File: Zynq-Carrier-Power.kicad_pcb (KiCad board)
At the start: 2 copper layers, 49 x 41 mm, 36 parts, among them J1 Zynq_SoM, J10 Barrel_Jack_MountingPin, J2 B2B-PH-K-S, J3 USB_C_Receptacle_USB2.0_16P, J4 Conn_01x03, J5 Conn_01x03, J6 Conn_01x03, J7 Conn_01x02, J8 Conn_01x02, J9 Conn_01x03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

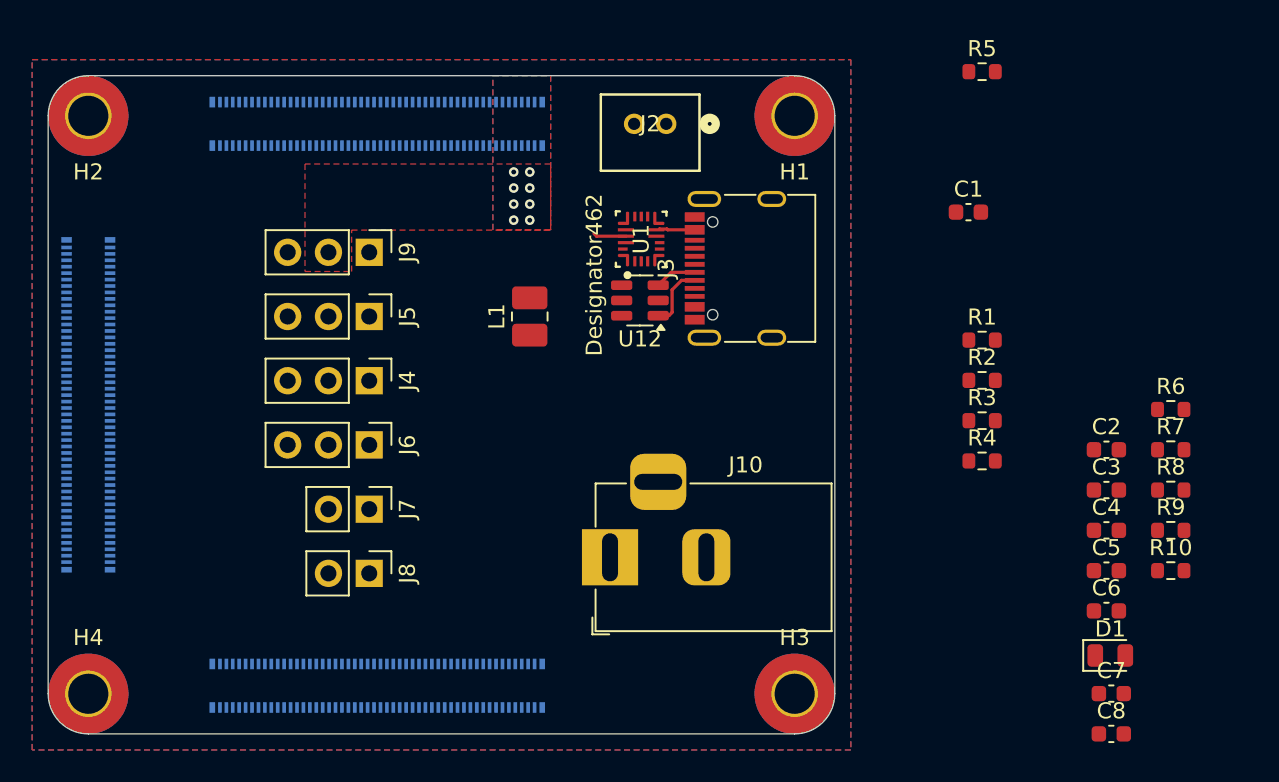
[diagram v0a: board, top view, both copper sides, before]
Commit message: Began work on PCB design for Zynq Carrier
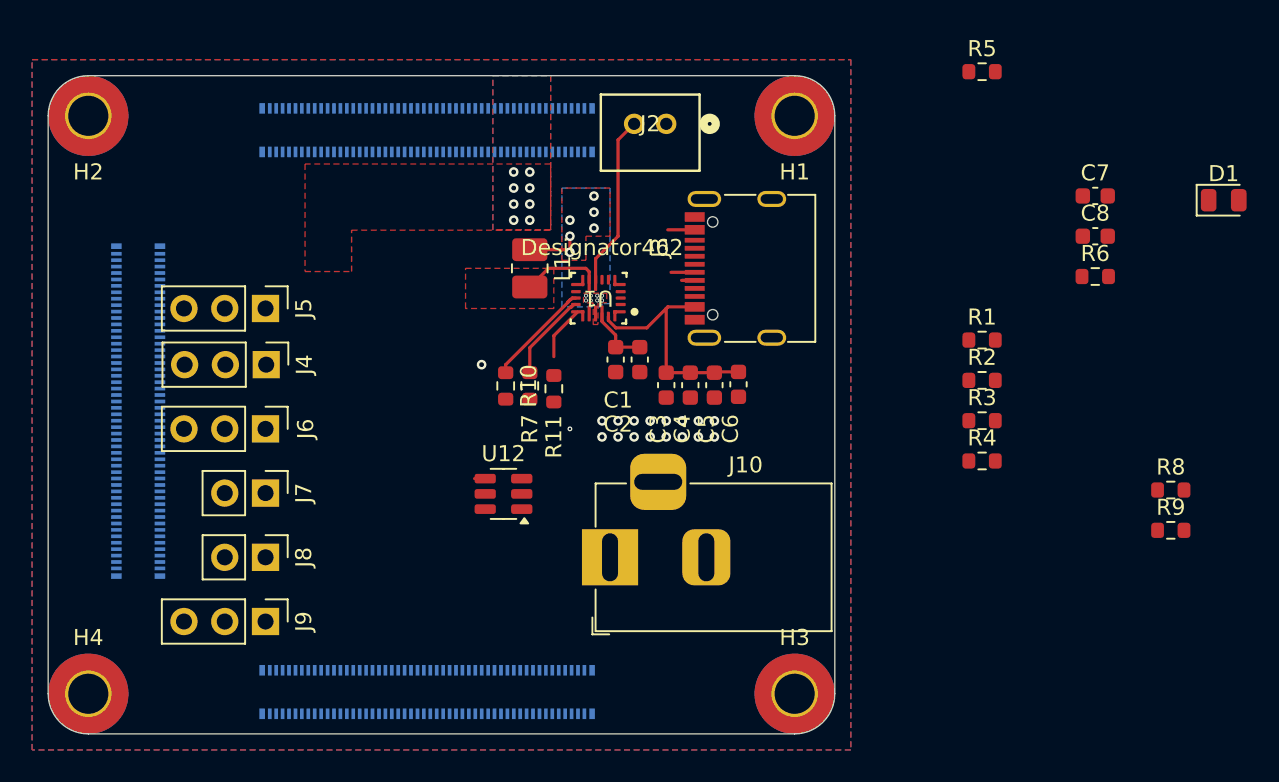
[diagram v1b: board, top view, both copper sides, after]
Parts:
- added R11: 4.7k, Resistor_SMD:R_0603_1608Metric, F.Cu at (128.7, 120.1)
- moved R10 43.0 mm to (125.7, 120.0), turned to -90 degrees
- moved R7 40.1 mm to (127.2, 120.0), turned to -90 degrees
- moved C8 31.0 mm to (162.5, 110.6)
- moved C7 31.0 mm to (162.5, 108.1)
- moved C2 29.6 mm to (134.1, 118.3), turned to -90 degrees
- moved D1 29.2 mm to (170.5, 108.4)
- moved C3 28.2 mm to (135.7, 119.9), turned to -90 degrees
- moved C4 27.5 mm to (137.2, 119.9), turned to -90 degrees
- moved C5 27.0 mm to (138.7, 119.9), turned to -90 degrees
- moved C6 26.9 mm to (140.2, 119.9), turned to -90 degrees
- moved J9 23.9 mm to (110.8, 134.6)
- moved C1 23.8 mm to (132.6, 118.3), turned to -90 degrees
- moved U12 14.7 mm to (125.6, 126.7)
- moved R6 9.52 mm to (162.5, 113.2)
- moved J6 6.54 mm to (110.8, 122.6)
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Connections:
- net Net-(U1-SW) renamed /SW
- H1 pad 1: unconnected-(H1-Pad1) -> GND
- H2 pad 1: unconnected-(H2-Pad1) -> GND
- H3 pad 1: unconnected-(H3-Pad1) -> GND
- H4 pad 1: unconnected-(H4-Pad1) -> GND
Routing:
- net V_USB: track 2.24 -> 16.6 mm
- net VBAT: track 0.00 -> 10.9 mm
- net /SDA: track 0.00 -> 6.61 mm
- net /SCL: track 0.00 -> 5.54 mm
- net VREG_OUT: track 0.00 -> 4.97 mm
- net Net-(U1-PMID): track 0.00 -> 4.21 mm
- net /~{CSn}: track 0.00 -> 3.40 mm
- net /USB_D-: track 4.01 -> 0.82 mm
- net /SW: track 2.06 -> 3.57 mm, vias 0 -> 14
- net /USB_D+: track 2.61 -> 1.47 mm
- net unconnected-(U12-IO3-Pad4): track 0.00 -> 0.66 mm
- net GND: vias 0 -> 18
- added copper zone on B.Cu, net /SW
- added copper zone on F.Cu, net /SW
- added copper zone on F.Cu, net VREG_OUT

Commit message: Updated PCB components
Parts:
- moved D1 46.3 mm to (125.8, 120.6), turned to 90 degrees
- moved R6 36.9 mm to (125.8, 117.2), turned to -90 degrees
- moved R11 2.91 mm to (131.0, 118.4)
- moved R7 2.73 mm to (129.5, 118.4)
- moved R10 2.73 mm to (128.0, 118.4)
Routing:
- net +5V: track 0.00 -> 22.2 mm, vias 8 -> 9
- net Net-(U1-STAT): track 0.00 -> 5.55 mm
- net /SDA: track 6.61 -> 4.17 mm
- net /SCL: track 5.54 -> 3.13 mm
- net Net-(D1-A): track 0.00 -> 1.65 mm
- net /~{CSn}: track 3.40 -> 2.15 mm
- net VBAT: track 10.9 -> 11.6 mm
- net GND: vias 18 -> 17

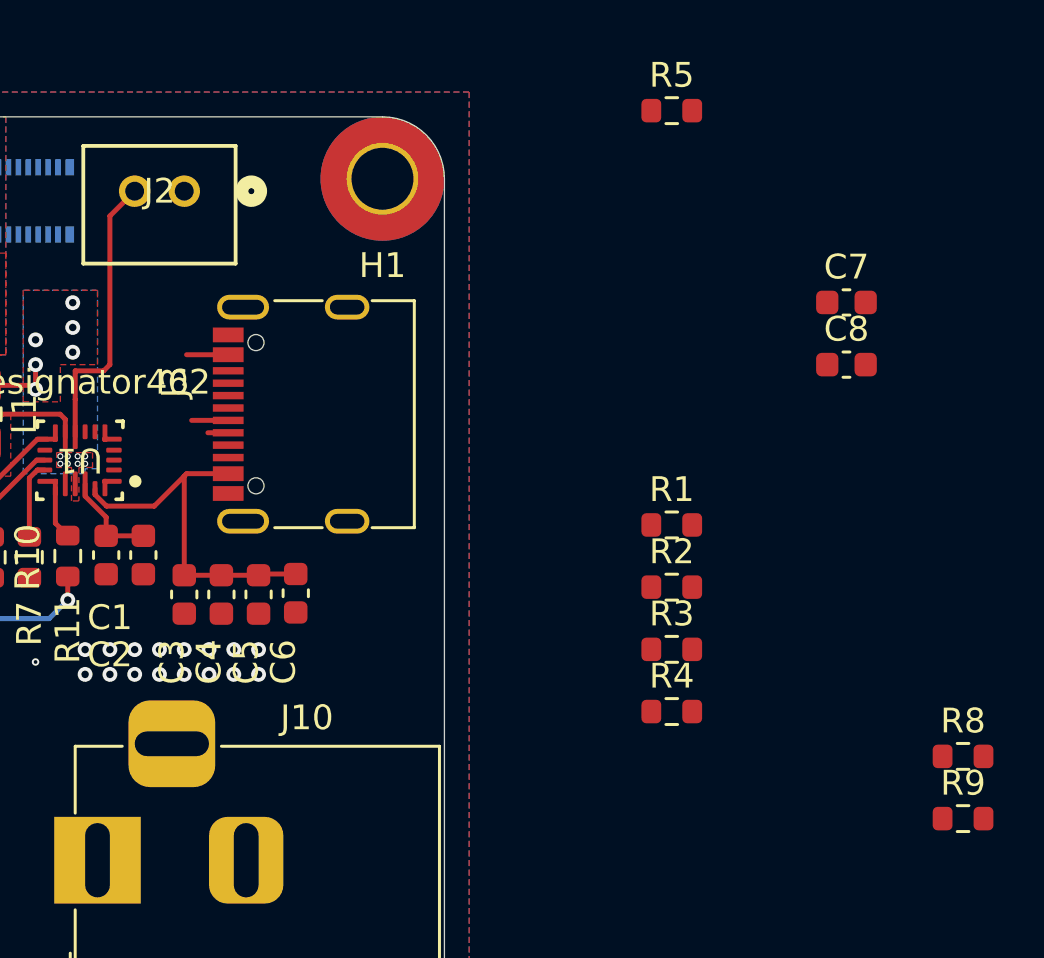
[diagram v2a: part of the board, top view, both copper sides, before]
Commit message: resolved drc errors
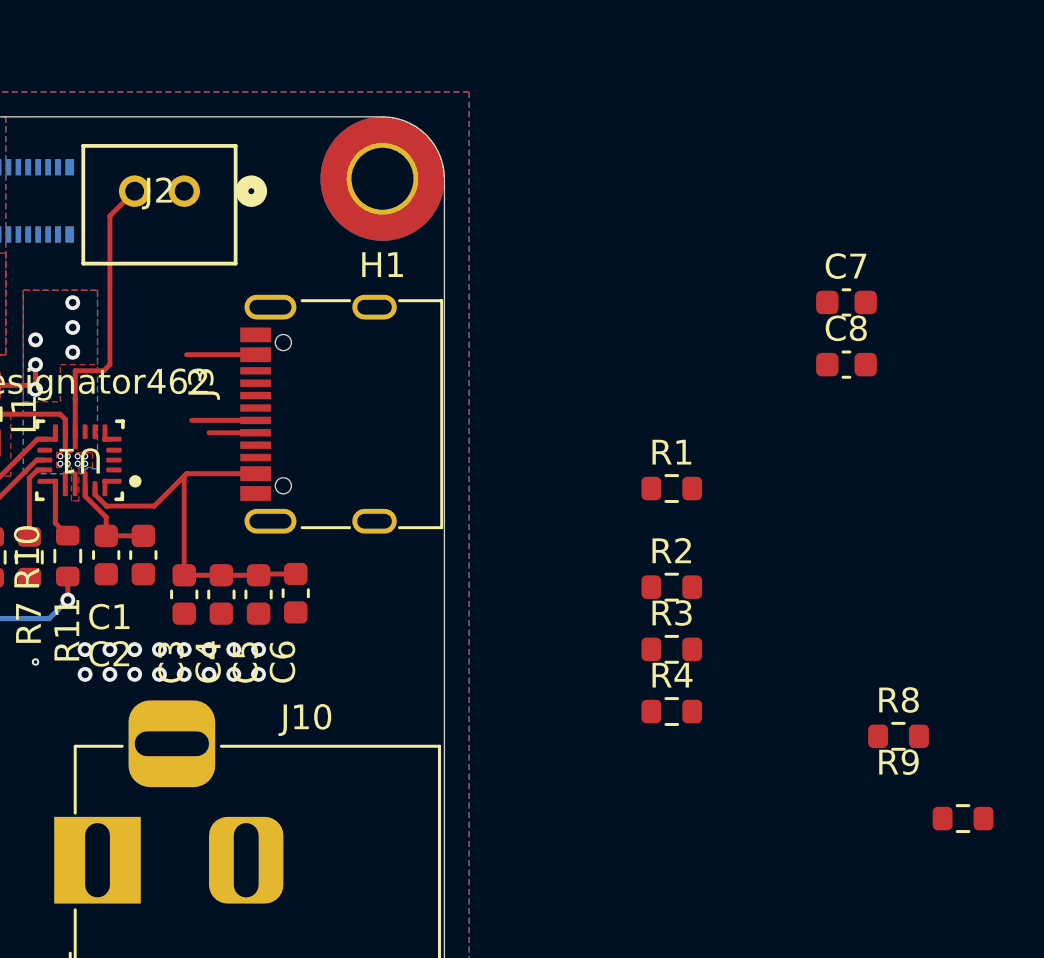
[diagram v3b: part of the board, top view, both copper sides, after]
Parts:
- removed R5: 100k, Resistor_SMD:R_0603_1608Metric
- moved R8 2.73 mm to (164.6, 125.6)
- moved R1 1.47 mm to (155.4, 115.6)
- moved J3 1.10 mm to (142.3, 112.6)
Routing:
- net V_USB: track 16.6 -> 18.8 mm
- net /USB_D+: track 1.47 -> 2.58 mm
- net /USB_D-: track 0.82 -> 1.88 mm
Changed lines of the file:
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@@
 	(footprint "Connector_USB:USB_C_Receptacle_G-Switch_GT-USB-7010ASV"
 		(layer "F.Cu")
-		(at 141.225004 112.645 90)
+		(at 142.330004 112.645 90)
 		(descr "USB Type C, right-angle, SMT, https://datasheet.lcsc.com/lcsc/2204071530_G-Switch-GT-USB-7010ASV_C2988369.pdf")
 		(tags "USB C Type-C Receptacle SMD")
@@
 	(footprint "Resistor_SMD:R_0603_1608Metric"
 		(layer "F.Cu")
-		(at 167.155004 126.455)
+		(at 164.550004 125.645)
 		(descr "Resistor SMD 0603 (1608 Metric), square (rectangular) end terminal, IPC-7351 nominal, (Body size source: IPC-SM-782 page 72, https://www.pcb-3d.com/wordpress/wp-content/uploads/ipc-sm-782a_amendment_1_and_2.pdf), generated with kicad-footprint-generator")
 		(tags "resistor")
@@
 		)
 	)
-	(footprint "Resistor_SMD:R_0603_1608Metric"
-		(layer "F.Cu")
-		(at 155.400004 100.395)
-		(descr "Resistor SMD 0603 (1608 Metric), square (rectangular) end terminal, IPC-7351 nominal, (Body size source: IPC-SM-782 page 72, https://www.pcb-3d.com/wordpress/wp-content/uploads/ipc-sm-782a_amendment_1_and_2.pdf), generated with kicad-footprint-generator")
-		(tags "resistor")
-		(property "Reference" "R5"
-			(at 0 -1.43 0)
-			(layer "F.SilkS")
-			(effects
-				(font
-					(size 1 1)
-					(thickness 0.15)
-				)
-			)
-		)
-		(property "Value" "100k"
-			(at 0 1.43 0)
-			(layer "F.Fab")
-			(effects
-				(font
-					(size 1 1)
-					(thickness 0.15)
-				)
-			)
-		)
-		(property "Datasheet" "~"
-			(at 0 0 0)
-			(layer "F.Fab")
-			(hide yes)
-			(effects
-				(font
-					(size 1.27 1.27)
-					(thickness 0.15)
-				)
-			)
-		)
-		(property "Description" "Resistor, US symbol"
-			(at 0 0 0)
-			(layer "F.Fab")
-			(hide yes)
-			(effects
-				(font
-					(size 1.27 1.27)
-					(thickness 0.15)
-				)
-			)
-		)
-		(property ki_fp_filters "R_*")
-		(sheetname "/")
-		(sheetfile "Zynq-Carrier-Power.kicad_sch")
-		(attr smd)
-		(fp_line
-			(start -0.237258 -0.5225)
-			(end 0.237258 -0.5225)
-			(stroke
-				(width 0.12)
-				(type solid)
-			)
-			(layer "F.SilkS")
-		)
-		(fp_line
-			(start -0.237258 0.5225)
-			(end 0.237258 0.5225)
-			(stroke
-				(width 0.12)
-				(type solid)
-			)
-			(layer "F.SilkS")
-		)
-		(fp_line
-			(start -1.48 -0.73)
-			(end 1.48 -0.73)
-			(stroke
-				(width 0.05)
-				(type solid)
-			)
-			(layer "F.CrtYd")
-		)
-		(fp_line
-			(start -1.48 0.73)
-			(end -1.48 -0.73)
-			(stroke
-				(width 0.05)
-				(type solid)
-			)
-			(layer "F.CrtYd")
-		)
-		(fp_line
-			(start 1.48 -0.73)
-			(end 1.48 0.73)
-			(stroke
-				(width 0.05)
-				(type solid)
-			)
-			(layer "F.CrtYd")
-		)
-		(fp_line
-			(start 1.48 0.73)
-			(end -1.48 0.73)
-			(stroke
-				(width 0.05)
-				(type solid)
-			)
-			(layer "F.CrtYd")
-		)
-		(fp_line
-			(start -0.8 -0.4125)
-			(end 0.8 -0.4125)
-			(stroke
-				(width 0.1)
-				(type solid)
-			)
-			(layer "F.Fab")
-		)
-		(fp_line
-			(start -0.8 0.4125)
-			(end -0.8 -0.4125)
-			(stroke
-				(width 0.1)
-				(type solid)
-			)
-			(layer "F.Fab")
-		)
-		(fp_line
-			(start 0.8 -0.4125)
-			(end 0.8 0.4125)
-			(stroke
-				(width 0.1)
-				(type solid)
-			)
-			(layer "F.Fab")
-		)
-		(fp_line
-			(start 0.8 0.4125)
-			(end -0.8 0.4125)
-			(stroke
-				(width 0.1)
-				(type solid)
-			)
-			(layer "F.Fab")
-		)
-		(fp_text user "${REFERENCE}"
-			(at 0 0 0)
-			(layer "F.Fab")
-			(effects
-				(font
-					(size 0.4 0.4)
-					(thickness 0.06)
-				)
-			)
-		)
-		(pad "1" smd roundrect
-			(at -0.825 0)
-			(size 0.8 0.95)
-			(layers "F.Cu" "F.Mask" "F.Paste")
-			(roundrect_rratio 0.25)
-			(net 19 "V_USB")
-			(pintype "passive")
-		)
-		(pad "2" smd roundrect
-			(at 0.825 0)
-			(size 0.8 0.95)
-			(layers "F.Cu" "F.Mask" "F.Paste")
-			(roundrect_rratio 0.25)
-			(net 252 "GND")
-			(pintype "passive")
-		)
-		(embedded_fonts no)
-		(model "${KICAD9_3DMODEL_DIR}/Resistor_SMD.3dshapes/R_0603_1608Metric.step"
-			(offset
-				(xyz 0 0 0)
-			)
-			(scale
-				(xyz 1 1 1)
-			)
-			(rotate
-				(xyz 0 0 0)
-			)
-		)
-	)
 	(footprint "Connector_PinHeader_2.54mm:PinHeader_1x02_P2.54mm_Vertical"
 		(layer "F.Cu")
@@
 	(footprint "Resistor_SMD:R_0603_1608Metric"
 		(layer "F.Cu")
-		(at 155.400004 117.115)
+		(at 155.400004 115.645)
 		(descr "Resistor SMD 0603 (1608 Metric), square (rectangular) end terminal, IPC-7351 nominal, (Body size source: IPC-SM-782 page 72, https://www.pcb-3d.com/wordpress/wp-content/uploads/ipc-sm-782a_amendment_1_and_2.pdf), generated with kicad-footprint-generator")
 		(tags "resistor")
@@
 		(tags "resistor")
 		(property "Reference" "R9"
-			(at 0 -1.43 0)
+			(at -2.605 -2.24 0)
 			(layer "F.SilkS")
 			(effects
@@
 	)
 	(segment
-		(start 137.500004 112.895)
+		(start 138.605004 112.895)
 		(end 136.025004 112.895)
 		(width 0.2)
@@
 	)
 	(segment
-		(start 137.500004 113.395)
-		(end 136.680004 113.395)
+		(start 138.605004 113.395)
+		(end 136.725004 113.395)
 		(width 0.2)
 		(layer "F.Cu")
@@
 	)
 	(segment
-		(start 135.825004 115.045)
-		(end 135.725004 115.145)
+		(start 138.725004 119.145)
+		(end 137.225004 119.145)
 		(width 0.2)
 		(layer "F.Cu")
@@
 	)
 	(segment
-		(start 138.725004 119.145)
-		(end 137.225004 119.145)
+		(start 135.820004 110.245)
+		(end 138.605004 110.245)
 		(width 0.2)
 		(layer "F.Cu")
@@
 	)
 	(segment
-		(start 135.820004 110.245)
-		(end 137.500004 110.245)
-		(width 0.2)
-		(layer "F.Cu")
-		(net 19)
-	)
-	(segment
-		(start 137.500004 115.045)
-		(end 135.825004 115.045)
+		(start 135.825004 115.045)
+		(end 138.605004 115.045)
 		(width 0.2)
 		(layer "F.Cu")
@@
 	)
 	(segment
+		(start 135.725004 115.145)
+		(end 135.825004 115.045)
+		(width 0.2)
+		(layer "F.Cu")
+		(net 19)
+	)
+	(segment
 		(start 123.787505 125.745)
 		(end 124.450004 125.745)
@@
 		(polygon
 			(pts
-				(xy 136.730004 112.795) (xy 136.730004 112.995) (xy 136.880004 113.045) (xy 137.501004 112.895)
-				(xy 136.880004 112.745)
+				(xy 137.835004 112.795) (xy 137.835004 112.995) (xy 137.985004 113.045) (xy 138.606004 112.895)
+				(xy 137.985004 112.745)
 			)
 		)
 	)
 	(zone
-		(net 267)
-		(net_name "VREG_OUT")
+		(net 14)
+		(net_name "/USB_D-")
 		(layer "F.Cu")
-		(hatch edge 0.5)
-		(priority 6)
-		(connect_pads
-			(clearance 0.1524)
+		(name "$teardrop_padvia$")
+		(hatch none 0.1)
+		(priority 30005)
+		(attr
+			(teardrop
+				(type padvia)
+			)
 		)
-		(min_thickness 0.25)
+		(connect_pads yes
+			(clearance 0)
+		)
+		(min_thickness 0.0254)
 		(filled_areas_thickness no)
 		(fill yes
 			(thermal_gap 0.5)
 			(thermal_bridge_width 0.5)
+			(island_removal_mode 1)
+			(island_area_min 10)
 		)
 		(polygon
 			(pts
-				(xy 128.725004 112.645) (xy 128.725004 115.145) (xy 123.225004 115.145) (xy 123.225004 112.645)
+				(xy 137.835004 113.295) (xy 137.835004 113.495) (xy 137.985004 113.545) (xy 138.606004 113.395)
+				(xy 137.985004 113.245)
 			)
 		)
 	)
 	(zone
-		(net 14)
-		(net_name "/USB_D-")
+		(net 19)
+		(net_name "V_USB")
 		(layer "F.Cu")
 		(name "$teardrop_padvia$")
 		(hatch none 0.1)
-		(priority 30005)
+		(priority 30002)
 		(attr
 			(teardrop
@@
 		(polygon
 			(pts
-				(xy 136.730004 113.295) (xy 136.730004 113.495) (xy 136.880004 113.545) (xy 137.501004 113.395)
-				(xy 136.880004 113.245)
+				(xy 137.685004 114.945) (xy 137.685004 115.145) (xy 137.985004 115.345) (xy 138.606004 115.045)
+				(xy 137.985004 114.745)
 			)
 		)
@@
 		(polygon
 			(pts
-				(xy 136.580004 114.945) (xy 136.580004 115.145) (xy 136.880004 115.345) (xy 137.501004 115.045)
-				(xy 136.880004 114.745)
+				(xy 137.685004 114.945) (xy 137.685004 115.145) (xy 137.985004 115.345) (xy 138.606004 115.045)
+				(xy 137.985004 114.745)
+			)
+		)
+	)
+	(zone
+		(net 267)
+		(net_name "VREG_OUT")
+		(layer "F.Cu")
+		(hatch edge 0.5)
+		(priority 6)
+		(connect_pads
+			(clearance 0.1524)
+		)
+		(min_thickness 0.25)
+		(filled_areas_thickness no)
+		(fill yes
+			(thermal_gap 0.5)
+			(thermal_bridge_width 0.5)
+		)
+		(polygon
+			(pts
+				(xy 128.725004 112.645) (xy 128.725004 115.145) (xy 123.225004 115.145) (xy 123.225004 112.645)
 			)
 		)
@@
 		(name "$teardrop_padvia$")
 		(hatch none 0.1)
-		(priority 30001)
+		(priority 30000)
 		(attr
 			(teardrop
@@
 		(polygon
 			(pts
-				(xy 136.580004 110.145) (xy 136.580004 110.345) (xy 136.880004 110.545) (xy 137.501004 110.245)
-				(xy 136.880004 109.945)
+				(xy 137.685004 110.145) (xy 137.685004 110.345) (xy 137.985004 110.545) (xy 138.606004 110.245)
+				(xy 137.985004 109.945)
 			)
 		)
@@
 		(name "$teardrop_padvia$")
 		(hatch none 0.1)
-		(priority 30002)
+		(priority 30001)
 		(attr
 			(teardrop
@@
 		(polygon
 			(pts
-				(xy 136.580004 114.945) (xy 136.580004 115.145) (xy 136.880004 115.345) (xy 137.501004 115.045)
-				(xy 136.880004 114.745)
+				(xy 137.685004 110.145) (xy 137.685004 110.345) (xy 137.985004 110.545) (xy 138.606004 110.245)
+				(xy 137.985004 109.945)
 			)
 		)
@@
 			)
 		)
-	)
-	(zone
-		(net 19)
-		(net_name "V_USB")
-		(layer "F.Cu")
-		(name "$teardrop_padvia$")
-		(hatch none 0.1)
-		(priority 30000)
-		(attr
-			(teardrop
-				(type padvia)
-			)
-		)
-		(connect_pads yes
-			(clearance 0)
-		)
-		(min_thickness 0.0254)
-		(filled_areas_thickness no)
-		(fill yes
-			(thermal_gap 0.5)
-			(thermal_bridge_width 0.5)
-			(island_removal_mode 1)
-			(island_area_min 10)
-		)
-		(polygon
-			(pts
-				(xy 136.580004 110.145) (xy 136.580004 110.345) (xy 136.880004 110.545) (xy 137.501004 110.245)
-				(xy 136.880004 109.945)
-			)
-		)
